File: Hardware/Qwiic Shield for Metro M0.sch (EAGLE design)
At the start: 14 parts, among them U1 ARDUINO UNO

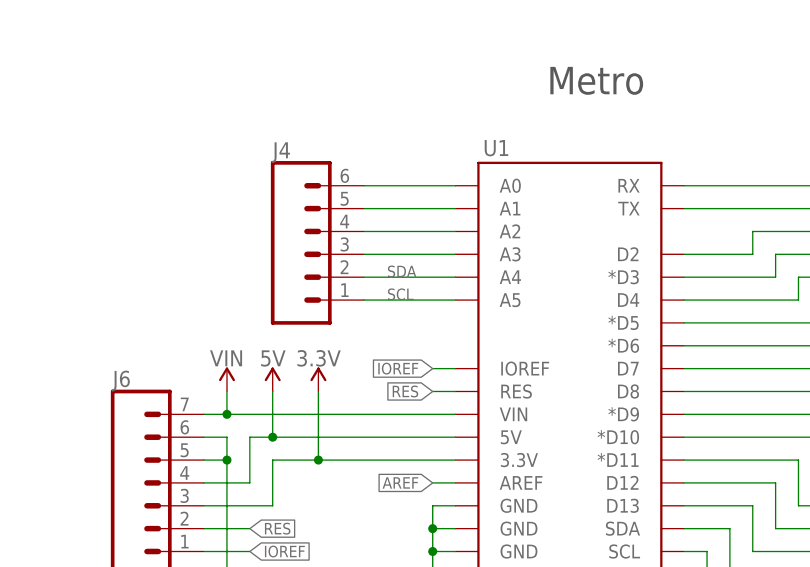
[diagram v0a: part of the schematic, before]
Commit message: Re-routed board to use SCL/SDA instead of A4/A5
The Metro Express M0 cannot use A4/A5 as SCL/SDA, so the previous
version of the shield was completely incompatible with the board.
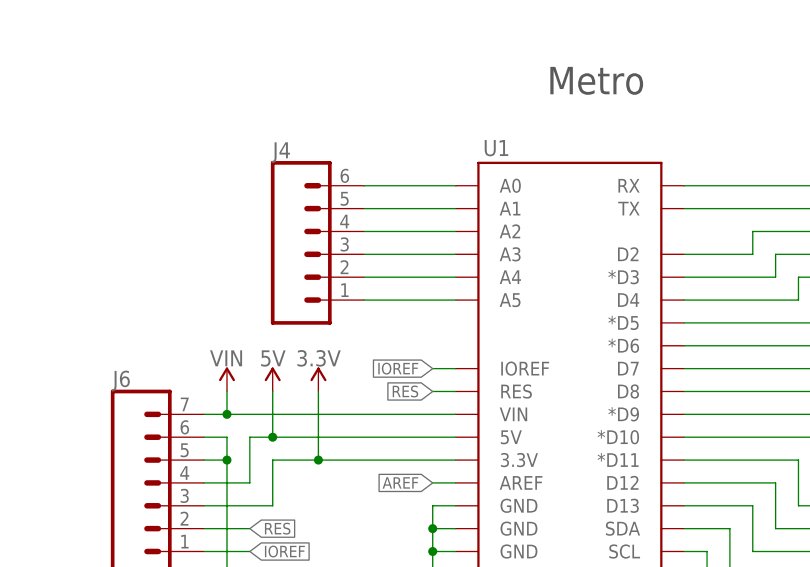
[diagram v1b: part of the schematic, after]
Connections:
- removed net SCL1: J3.10, U1.SCL
- removed net SDA1: J3.9, U1.SDA
- new net A4: J4.2, U1.A4
- new net A5: J4.1, U1.A5
- net SCL: now also J3.10, U1.SCL; no longer J4.1, U1.A5
- net SDA: now also J3.9, U1.SDA; no longer J4.2, U1.A4
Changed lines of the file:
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@@
 </segment>
 <segment>
-<pinref part="U1" gate="G$1" pin="A5"/>
-<pinref part="J4" gate="G$1" pin="1"/>
-<wire x1="132.08" y1="129.54" x2="142.24" y2="129.54" width="0.1524" layer="91"/>
-<label x="134.62" y="129.54" size="1.27" layer="95"/>
+<pinref part="J3" gate="G$1" pin="10"/>
+<wire x1="190.5" y1="91.44" x2="170.18" y2="91.44" width="0.1524" layer="91"/>
+<wire x1="170.18" y1="91.44" x2="170.18" y2="101.6" width="0.1524" layer="91"/>
+<pinref part="U1" gate="G$1" pin="SCL"/>
+<wire x1="170.18" y1="101.6" x2="167.64" y2="101.6" width="0.1524" layer="91"/>
 </segment>
 </net>
@@
 </segment>
 <segment>
-<pinref part="U1" gate="G$1" pin="A4"/>
-<pinref part="J4" gate="G$1" pin="2"/>
-<wire x1="132.08" y1="132.08" x2="142.24" y2="132.08" width="0.1524" layer="91"/>
-<label x="134.62" y="132.08" size="1.27" layer="95"/>
+<pinref part="U1" gate="G$1" pin="SDA"/>
+<wire x1="167.64" y1="104.14" x2="172.72" y2="104.14" width="0.1524" layer="91"/>
+<wire x1="172.72" y1="104.14" x2="172.72" y2="93.98" width="0.1524" layer="91"/>
+<pinref part="J3" gate="G$1" pin="9"/>
+<wire x1="172.72" y1="93.98" x2="190.5" y2="93.98" width="0.1524" layer="91"/>
 </segment>
 </net>
@@
 </segment>
 </net>
-<net name="SCL1" class="0">
-<segment>
-<pinref part="J3" gate="G$1" pin="10"/>
-<wire x1="190.5" y1="91.44" x2="170.18" y2="91.44" width="0.1524" layer="91"/>
-<wire x1="170.18" y1="91.44" x2="170.18" y2="101.6" width="0.1524" layer="91"/>
-<pinref part="U1" gate="G$1" pin="SCL"/>
-<wire x1="170.18" y1="101.6" x2="167.64" y2="101.6" width="0.1524" layer="91"/>
-</segment>
-</net>
-<net name="SDA1" class="0">
-<segment>
-<pinref part="U1" gate="G$1" pin="SDA"/>
-<wire x1="167.64" y1="104.14" x2="172.72" y2="104.14" width="0.1524" layer="91"/>
-<wire x1="172.72" y1="104.14" x2="172.72" y2="93.98" width="0.1524" layer="91"/>
-<pinref part="J3" gate="G$1" pin="9"/>
-<wire x1="172.72" y1="93.98" x2="190.5" y2="93.98" width="0.1524" layer="91"/>
-</segment>
-</net>
+<net name="A5" class="0">
+<segment>
+<pinref part="U1" gate="G$1" pin="A5"/>
+<pinref part="J4" gate="G$1" pin="1"/>
+<wire x1="132.08" y1="129.54" x2="142.24" y2="129.54" width="0.1524" layer="91"/>
+</segment>
+</net>
+<net name="A4" class="0">
+<segment>
+<pinref part="U1" gate="G$1" pin="A4"/>
+<pinref part="J4" gate="G$1" pin="2"/>
+<wire x1="132.08" y1="132.08" x2="142.24" y2="132.08" width="0.1524" layer="91"/>
+</segment>
+</net>
